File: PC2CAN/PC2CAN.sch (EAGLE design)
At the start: 97 parts, among them J11 M10X2, Q1 INFINEON_2N7002_DW, Q2 INFINEON_2N7002_DW, Q3 BS250F, Q4 BS250F, Q5 INFINEON_2N7002_DW, Q6 INFINEON_2N7002_DW, Q7 INFINEON_2N7002_DW, U1 MSP430F5521/5/7/9_PN80, U2 LTV-817, U3 SN74LV74, U4 SN74LV08

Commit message: Removed irrelevant circuits for PC2CAN and Power Controller
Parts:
- removed C11, C12: 0.1uF, rcl:C-USC0603
- removed JP10, JP11, JP13: M023.5MM, SparkFun-Connectors:M023.5MM
- removed JP14, JP7: (no value), SparkFun-Connectors:M04SCREW
- removed JP15: (no value), SparkFun-Connectors:M07
- removed JP6: (no value), SparkFun-Connectors:M05LOCK
- removed JP8: M02LOCK, SparkFun-Connectors:M02LOCK
- removed LED10, LED11, LED8, LED9: (no value), SparkFun-LED:LED0603
- removed Q1, Q6, Q7: INFINEON_2N7002_DW, npol-discrete:INFINEON_2N7002_DW
- removed R13, R27, R28, R33, R34: 0, rcl:R-US_R0603
- removed R23, R24: 10k, rcl:R-US_R0603
- removed R29, R30, R31, R32: 1k, rcl:R-US_R0603
- removed U3: SN74LV74, npol-digital:SN74LV74
- removed U4: SN74LV08, npol-digital:SN74LV08
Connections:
- removed net DRILL_RELAY_1: JP14.4, Q6G$1.DRAIN
- removed net DRILL_RELAY_2: JP14.3, Q6G$2.DRAIN
- removed net DRILL_RELAY_3: JP14.2, Q7G$1.DRAIN
- removed net DRILL_RELAY_4: JP14.1, Q7G$2.DRAIN
- removed net ESTOP_RELAY: JP13.2, Q1G$1.SOURCE, Q1G$2.SOURCE
- removed net N$14: LED9.A, R30.1
- removed net N$20: U31.Q, U41.A
- removed net N$22: U31./Q, U42.B
- removed net N$23: U32.Q, U43.A
- removed net N$25: U32./Q, U44.B
- removed net N$26: R27.1, U31./PRE
- removed net N$27: R28.2, U31./CLR
- removed net N$28: R33.1, U32./PRE
- removed net N$29: R34.2, U32./CLR
- removed net N$33: LED11.A, R32.1
- removed net RC_PWR: JP6.2, JP8.1
- removed net RC_S3: JP6.5, R13.2
- removed net RELAY1_CNTRL: Q6G$1.GATE, R29.2, U41.Y
- removed net RELAY1_LED_A: LED8.A, R29.1
- removed net RELAY2_CNTRL: Q6G$2.GATE, R30.2, U42.Y
- removed net RELAY3_CNTRL: Q7G$1.GATE, R31.2, U43.Y
- removed net RELAY3_LED_A: LED10.A, R31.1
- removed net RELAY4_CNTRL: Q7G$2.GATE, R32.2, U44.Y
- removed net VOC: JP15.7
- net +12V: no longer JP13.1
- net +3V3: no longer C11.1, C12.1, JP15.2, R23.2, R24.2, R27.2, R28.1, R33.2, R34.1, U31.VCC, U41.VCC
- net +5V: no longer JP7.4, JP8.2
- net DRILL_EN: no longer U31.CLK, U32.CLK, U41.B, U42.A, U43.B, U44.A
- net DRILL_ISENSE_/FAULT: no longer JP15.5
- net DRILL_ISENSE_FAULT_EN: no longer JP15.6
- net DRILL_ISENSE_VIOUT: no longer JP15.3
- net DRILL_ISENSE_VZCR: no longer JP15.4
- net DRILL_S1: no longer U31.D
- net DRILL_S2: no longer U32.D
- net ESTOP_LOCAL: no longer Q1G$1.GATE, Q1G$2.GATE, R13.1
- net GND: no longer C11.2, C12.2, JP10.1, JP11.1, JP15.1, JP6.1, LED10.C, LED11.C, LED8.C, LED9.C, Q1G$1.DRAIN, Q1G$2.DRAIN, Q6G$1.SOURCE, Q6G$2.SOURCE, Q7G$1.SOURCE, Q7G$2.SOURCE, U31.GND, U41.GND
- net LOWER_SWITCH: no longer JP11.2, R24.1
- net RC_S1: no longer JP6.3
- net RC_S2: no longer JP6.4
- net STEPPER_DIR: no longer JP7.2
- net STEPPER_EN: no longer JP7.3
- net STEPPER_STEP: no longer JP7.1
- net UPPER_SWITCH: no longer JP10.2, R23.1
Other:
- note added: "TODO: FTDI"
- note removed: "ACS709 Current Sensor"
- note removed: "ESTOP Relay Output shared with Drill and Stepper ESTOP relays"
- note removed: "Limit switches"
- note removed: "Roboclaw"
- note removed: "Stepper driver"
- note removed: "VOC Unused"

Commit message: PC2CAN ready for fab
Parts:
- removed JP12: M02LOCK, SparkFun-Connectors:M02LOCK
- removed Q5: INFINEON_2N7002_DW, npol-discrete:INFINEON_2N7002_DW
- added C11: 10nF, rcl:C-USC0603
- added C12: 0.1uF, rcl:C-USC0603
- added JP6: (no value), SparkFun-Connectors:M03LOCK
- added JP7: USB-B, SparkFun-Connectors:USBPTH
- added JP8: M02POLAR_LOCK, SparkFun-Connectors:M02POLAR_LOCK
- added LED10, LED8, LED9: (no value), SparkFun-LED:LED0603
- added Q1: INFINEON_2N7002_DW, npol-discrete:INFINEON_2N7002_DW
- added R13, R23: 10k, rcl:R-US_R0603
- added R24: 620, rcl:R-US_R0603
- added U3: LTV-817, npol-digital:LTV-817
- JP1: device SparkFun-Connectors:M03X22X3_SILK_SM -> SparkFun-Connectors:M05PTH
- JP2: value M02LOCK -> (none); device SparkFun-Connectors:M02LOCK -> SparkFun-Connectors:M03X22X3_SILK_SM
- JP3: value ONSHORE_OST302-S141 -> M02LOCK; device npol-connectors:ONSHORE_OST302-S141 -> SparkFun-Connectors:M02LOCK
- JP4: value FTDI_DEVICE -> ONSHORE_OST302-S141; device SparkFun-Connectors:FTDI_DEVICE -> npol-connectors:ONSHORE_OST302-S141
- JP5: value (none) -> FTDI_DEVICE; device SparkFun-Connectors:M03LOCK -> SparkFun-Connectors:FTDI_DEVICE
- JP9: value M02POLAR_LOCK -> M02LOCK; device SparkFun-Connectors:M02POLAR_LOCK -> SparkFun-Connectors:M02LOCK
- Q2: value INFINEON_2N7002_DW -> BS250F; device npol-discrete:INFINEON_2N7002_DW -> SparkFun-DiscreteSemi:MOSFET-PCHANNELSMD
- Q4: value BS250F -> INFINEON_2N7002_DW; device SparkFun-DiscreteSemi:MOSFET-PCHANNELSMD -> npol-discrete:INFINEON_2N7002_DW
- R15, R17: value 10k -> 470
- R18, R21: value 100k -> 10k
- R20, R22: value 10k -> 100k
- R25: value 620 -> 10k
- U2: value LTV-817 -> FT232RLSSOP; device npol-digital:LTV-817 -> SparkFun-DigitalIC:FT232RLSSOP
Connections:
- removed net DRILL_EN: U1.P7.6/TB0.4
- removed net DRILL_ISENSE_/FAULT: U1.P1.3/TA0.2
- removed net DRILL_ISENSE_FAULT_EN: U1.P6.0/CB0/A0
- removed net DRILL_ISENSE_VIOUT: U1.P6.2/CB2/A2
- removed net DRILL_ISENSE_VZCR: U1.P6.1/CB1/A1
- removed net DRILL_S1: U1.P7.5/TB0.3
- removed net DRILL_S2: U1.P7.4/TB0.2
- removed net LOWER_SWITCH: U1.P2.0/TA1.1
- removed net RC_RXD: R14.2, SJ3.3, SJ4.1, U1.P4.5/PM_UCA1RXD/PM_UCA1SOMI
- removed net RC_S1: SJ3.2
- removed net RC_S2: SJ4.2
- removed net RC_TXD: R15.2, SJ3.1, SJ4.3, U1.P4.4/PM_UCA1TXD/PM_UCA1SIMO
- removed net STEPPER_DIR: U1.P7.1/CB9/A13
- removed net STEPPER_EN: U1.P7.2/CB10/A14
- removed net STEPPER_STEP: U1.P1.2/TA0.1
- removed net UPPER_SWITCH: U1.P2.1/TA1.2
- new net N$14: JP7.D+, U2.USBDP
- new net N$15: JP7.D-, U2.USBDM
- new net N$16: LED8.C, R15.2
- new net N$17: LED9.C, R17.2
- new net N$18: R15.1, U2.TXLED
- new net N$19: R17.1, U2.RXLED
- new net N$20: C12.1, U2.3V3OUT
- new net N$21: Q4G$2.DRAIN, R26.2
- new net N$22: LED10.C, R26.1
- new net NU_P3.7: JP1.5, U1.P3.7/TB0OUTH/SVMOUT
- new net NU_P4.0: JP1.4, U1.P4.0/PM_UCB1STE/PM_UCA1CLK
- new net NU_P4.1: JP1.3, U1.P4.1/PM_UCB1SIMO/PM_UCB1SDA
- new net NU_P4.2: JP1.2, U1.P4.2/PM_UCB1SOMI/PM_UCB1SCL
- new net NU_P4.3: JP1.1, U1.P4.3/PM_UCB1CLK/PM_UCA1STE
- new net USB_RX: SJ3.2, U2.TXD
- new net USB_RXD: R13.2, SJ3.3, SJ4.1, U1.P4.5/PM_UCA1RXD/PM_UCA1SOMI
- new net USB_TX: SJ4.2, U2.RXD
- new net USB_TXD: R14.2, SJ3.1, SJ4.3, U1.P4.4/PM_UCA1TXD/PM_UCA1SIMO
- new net VBUS: C11.1, JP7.VBUS, LED8.A, LED9.A, U2.VCC, U2.VCCIO
- net +12V: now also Q3.S, R21.2; no longer Q4.S, R20.2
- net +3V3: now also JP3.1, JP6.2, LED10.A, R25.1; no longer JP2.1, JP5.2, R26.1
- net +5V: now also Q2.S, R18.2; no longer Q3.S, R17.2
- net 12VSENSE: now also R22.1, R23.2; no longer R21.1, R22.2
- net 5VSENSE: now also R19.1, R20.2; no longer R18.1, R19.2
- net ESTOP+: now also JP8.1, R24.2; no longer JP9.1, R25.2
- net ESTOP-: now also JP8.2, U3.2; no longer JP9.2, U2.2
- net ESTOP_LOCAL: now also JP9.1, Q4G$1.DRAIN, Q4G$2.GATE, R25.2; no longer JP12.1, Q5G$1.DRAIN, R26.2
- net ESTOP_LOCAL_INV: now also Q4G$1.GATE, U3.4; no longer Q5G$1.GATE, U2.4
- net GND: now also C11.2, C12.2, JP2.2, JP4.9, JP5.GND, JP7.GND, JP9.2, Q1G$1.SOURCE, Q1G$2.SOURCE, Q4G$1.SOURCE, Q4G$2.SOURCE, R13.1, R20.1, R23.1, U2.AGND, U2.GND18, U2.GND21, U2.GND7, U2.TEST, U3.3; no longer JP1.2, JP12.2, JP3.9, JP4.GND, Q2G$1.SOURCE, Q2G$2.SOURCE, Q5G$1.SOURCE, R15.1, R19.1, R22.1, U2.3
- net N$1: now also JP3.2, JP5.VCC; no longer JP2.2, JP4.VCC
- net N$10: now also Q1G$1.DRAIN, Q2.G, R18.1; no longer Q2G$1.DRAIN, Q3.G, R17.1
- net N$11: now also Q3.D, R22.2; no longer Q4.D, R21.2
- net N$12: now also Q1G$1.GATE, Q1G$2.GATE; no longer Q2G$1.GATE, Q2G$2.GATE
- net N$13: now also R24.1, U3.1; no longer R25.1, U2.1
- net N$9: now also Q2.D, R19.2; no longer Q3.D, R18.2
- net NU_P6.3: now also JP2.5; no longer JP1.5
- net NU_P6.4: now also JP2.6; no longer JP1.6
- net NU_P6.5: now also JP2.3; no longer JP1.3
- net NU_P6.6: now also JP2.4; no longer JP1.4
- net NU_P6.7: now also JP2.1; no longer JP1.1
- net RXI: now also JP5.RXI; no longer JP4.RXI
- net SBWTCK: now also JP4.7; no longer JP3.7
- net SBWTDIO: now also JP4.1; no longer JP3.1
- net TXO: now also JP5.TXO; no longer JP4.TXO
- net VCC_TARGET: now also JP4.4, JP6.1; no longer JP3.4, JP5.1
- net VCC_TOOL: now also JP4.2, JP6.3; no longer JP3.2, JP5.3
- net VTAP_EN: now also Q1G$2.DRAIN, Q3.G, R21.1; no longer Q2G$2.DRAIN, Q4.G, R20.1
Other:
- note removed: "TODO: FTDI"
- moved on the sheet: JP9, Q3, R14, R15, R17, R18, R19, R20, R21, R22, R25, R26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

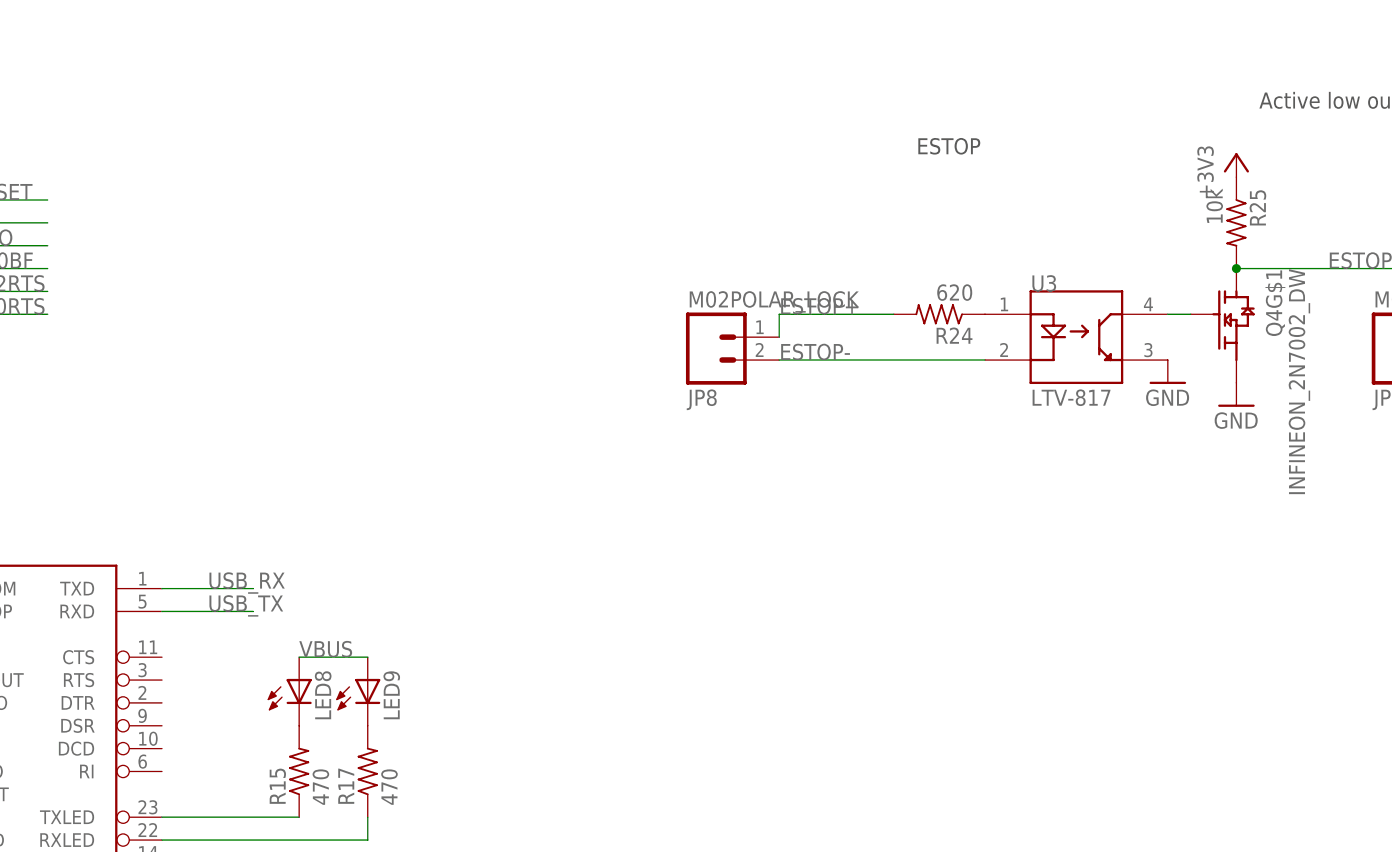
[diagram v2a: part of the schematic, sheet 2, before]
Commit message: Power Controller, Elim-Mobility Controller, and PC2CAN sent to FAB
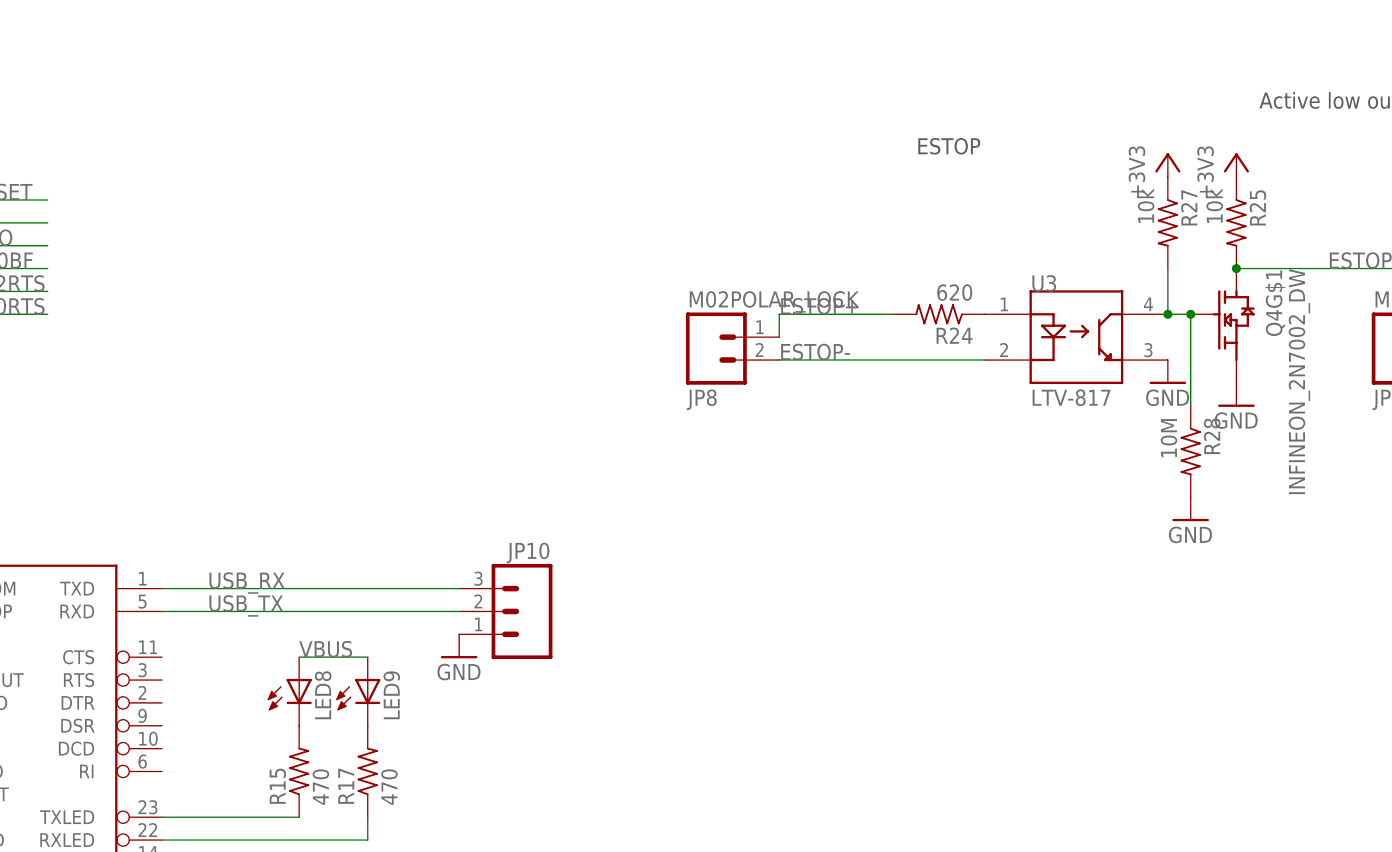
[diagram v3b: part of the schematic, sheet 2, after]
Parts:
- added JP10: (no value), SparkFun-Connectors:M03LOCK
- added R27: 10k, rcl:R-US_R0603
- added R28: 10M, rcl:R-US_R0603
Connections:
- net +3V3: now also R27.1
- net ESTOP_LOCAL_INV: now also R27.2, R28.1
- net GND: now also JP10.1, R28.2
- net USB_RX: now also JP10.3
- net USB_TX: now also JP10.2
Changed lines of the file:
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@@
 <grid distance="0.1" unitdist="inch" unit="inch" style="lines" multiple="1" display="no" altdistance="0.01" altunitdist="inch" altunit="inch"/>
 <layers>
-<layer number="1" name="Top" color="4" fill="1" visible="yes" active="no"/>
-<layer number="2" name="Route2" color="1" fill="3" visible="yes" active="no"/>
-<layer number="3" name="Route3" color="4" fill="3" visible="yes" active="no"/>
-<layer number="14" name="Route14" color="1" fill="6" visible="yes" active="no"/>
-<layer number="15" name="Route15" color="4" fill="6" visible="yes" active="no"/>
-<layer number="16" name="Bottom" color="1" fill="1" visible="yes" active="no"/>
-<layer number="17" name="Pads" color="2" fill="1" visible="yes" active="no"/>
-<layer number="18" name="Vias" color="2" fill="1" visible="yes" active="no"/>
-<layer number="19" name="Unrouted" color="6" fill="1" visible="yes" active="no"/>
-<layer number="20" name="Dimension" color="15" fill="1" visible="yes" active="no"/>
-<layer number="21" name="tPlace" color="7" fill="1" visible="yes" active="no"/>
-<layer number="22" name="bPlace" color="7" fill="1" visible="yes" active="no"/>
-<layer number="23" name="tOrigins" color="15" fill="1" visible="yes" active="no"/>
-<layer number="24" name="bOrigins" color="15" fill="1" visible="yes" active="no"/>
-<layer number="25" name="tNames" color="7" fill="1" visible="yes" active="no"/>
-<layer number="26" name="bNames" color="7" fill="1" visible="yes" active="no"/>
-<layer number="27" name="tValues" color="7" fill="1" visible="yes" active="no"/>
-<layer number="28" name="bValues" color="7" fill="1" visible="yes" active="no"/>
+<layer number="1" name="Top" color="4" fill="1" visible="no" active="no"/>
+<layer number="2" name="Route2" color="1" fill="3" visible="no" active="no"/>
+<layer number="3" name="Route3" color="4" fill="3" visible="no" active="no"/>
+<layer number="14" name="Route14" color="1" fill="6" visible="no" active="no"/>
+<layer number="15" name="Route15" color="4" fill="6" visible="no" active="no"/>
+<layer number="16" name="Bottom" color="1" fill="1" visible="no" active="no"/>
+<layer number="17" name="Pads" color="2" fill="1" visible="no" active="no"/>
+<layer number="18" name="Vias" color="2" fill="1" visible="no" active="no"/>
+<layer number="19" name="Unrouted" color="6" fill="1" visible="no" active="no"/>
+<layer number="20" name="Dimension" color="15" fill="1" visible="no" active="no"/>
+<layer number="21" name="tPlace" color="7" fill="1" visible="no" active="no"/>
+<layer number="22" name="bPlace" color="7" fill="1" visible="no" active="no"/>
+<layer number="23" name="tOrigins" color="15" fill="1" visible="no" active="no"/>
+<layer number="24" name="bOrigins" color="15" fill="1" visible="no" active="no"/>
+<layer number="25" name="tNames" color="7" fill="1" visible="no" active="no"/>
+<layer number="26" name="bNames" color="7" fill="1" visible="no" active="no"/>
+<layer number="27" name="tValues" color="7" fill="1" visible="no" active="no"/>
+<layer number="28" name="bValues" color="7" fill="1" visible="no" active="no"/>
 <layer number="29" name="tStop" color="7" fill="3" visible="no" active="no"/>
 <layer number="30" name="bStop" color="7" fill="6" visible="no" active="no"/>
@@
 <layer number="35" name="tGlue" color="7" fill="4" visible="no" active="no"/>
 <layer number="36" name="bGlue" color="7" fill="5" visible="no" active="no"/>
-<layer number="37" name="tTest" color="7" fill="1" visible="yes" active="no"/>
-<layer number="38" name="bTest" color="7" fill="1" visible="yes" active="no"/>
+<layer number="37" name="tTest" color="7" fill="1" visible="no" active="no"/>
+<layer number="38" name="bTest" color="7" fill="1" visible="no" active="no"/>
 <layer number="39" name="tKeepout" color="4" fill="11" visible="no" active="no"/>
 <layer number="40" name="bKeepout" color="1" fill="11" visible="no" active="no"/>
@@
 <layer number="44" name="Drills" color="7" fill="1" visible="no" active="no"/>
 <layer number="45" name="Holes" color="7" fill="1" visible="no" active="no"/>
-<layer number="46" name="Milling" color="3" fill="1" visible="yes" active="no"/>
-<layer number="47" name="Measures" color="7" fill="1" visible="yes" active="no"/>
-<layer number="48" name="Document" color="7" fill="1" visible="yes" active="no"/>
-<layer number="49" name="Reference" color="7" fill="1" visible="yes" active="no"/>
-<layer number="50" name="dxf" color="7" fill="1" visible="yes" active="no"/>
-<layer number="51" name="tDocu" color="7" fill="1" visible="yes" active="no"/>
-<layer number="52" name="bDocu" color="7" fill="1" visible="yes" active="no"/>
-<layer number="53" name="tGND_GNDA" color="7" fill="9" visible="yes" active="no"/>
-<layer number="54" name="bGND_GNDA" color="1" fill="9" visible="yes" active="no"/>
-<layer number="56" name="wert" color="7" fill="1" visible="yes" active="no"/>
-<layer number="57" name="tCAD" color="7" fill="1" visible="yes" active="no"/>
-<layer number="59" name="tCarbon" color="7" fill="1" visible="yes" active="no"/>
-<layer number="60" name="bCarbon" color="7" fill="1" visible="yes" active="no"/>
+<layer number="46" name="Milling" color="3" fill="1" visible="no" active="no"/>
+<layer number="47" name="Measures" color="7" fill="1" visible="no" active="no"/>
+<layer number="48" name="Document" color="7" fill="1" visible="no" active="no"/>
+<layer number="49" name="Reference" color="7" fill="1" visible="no" active="no"/>
+<layer number="50" name="dxf" color="7" fill="1" visible="no" active="no"/>
+<layer number="51" name="tDocu" color="7" fill="1" visible="no" active="no"/>
+<layer number="52" name="bDocu" color="7" fill="1" visible="no" active="no"/>
+<layer number="53" name="tGND_GNDA" color="7" fill="9" visible="no" active="no"/>
+<layer number="54" name="bGND_GNDA" color="1" fill="9" visible="no" active="no"/>
+<layer number="56" name="wert" color="7" fill="1" visible="no" active="no"/>
+<layer number="57" name="tCAD" color="7" fill="1" visible="no" active="no"/>
+<layer number="59" name="tCarbon" color="7" fill="1" visible="no" active="no"/>
+<layer number="60" name="bCarbon" color="7" fill="1" visible="no" active="no"/>
 <layer number="91" name="Nets" color="2" fill="1" visible="yes" active="yes"/>
 <layer number="92" name="Busses" color="1" fill="1" visible="yes" active="yes"/>
@@
 <part name="+3V39" library="supply1" deviceset="+3V3" device=""/>
 <part name="R26" library="rcl" deviceset="R-US_" device="R0603" value="10k"/>
+<part name="R27" library="rcl" deviceset="R-US_" device="R0603" value="10k"/>
+<part name="R28" library="rcl" deviceset="R-US_" device="R0603" value="10M"/>
+<part name="GND40" library="supply1" deviceset="GND" device=""/>
+<part name="+3V1" library="supply1" deviceset="+3V3" device=""/>
+<part name="JP10" library="SparkFun-Connectors" deviceset="M03" device="LOCK"/>
+<part name="GND41" library="supply1" deviceset="GND" device=""/>
 </parts>
 <sheets>
@@
 <instance part="+3V39" gate="G$1" x="248.92" y="208.28"/>
 <instance part="R26" gate="G$1" x="248.92" y="193.04" rot="R270"/>
+<instance part="R27" gate="G$1" x="200.66" y="187.96" rot="R270"/>
+<instance part="R28" gate="G$1" x="203.2" y="162.56" rot="R270"/>
+<instance part="GND40" gate="1" x="203.2" y="154.94"/>
+<instance part="+3V1" gate="G$1" x="200.66" y="195.58"/>
+<instance part="JP10" gate="G$1" x="129.54" y="144.78" rot="MR0"/>
+<instance part="GND41" gate="1" x="121.92" y="139.7"/>
 </instances>
 <busses>
@@
 <pinref part="GND39" gate="1" pin="GND"/>
 </segment>
+<segment>
+<pinref part="R28" gate="G$1" pin="2"/>
+<pinref part="GND40" gate="1" pin="GND"/>
+</segment>
+<segment>
+<pinref part="JP10" gate="G$1" pin="1"/>
+<pinref part="GND41" gate="1" pin="GND"/>
+</segment>
 </net>
 <net name="CAN_STBY" class="0">
@@
 <pinref part="+3V39" gate="G$1" pin="+3V3"/>
 <pinref part="LED10" gate="G$1" pin="A"/>
+</segment>
+<segment>
+<pinref part="R27" gate="G$1" pin="1"/>
+<pinref part="+3V1" gate="G$1" pin="+3V3"/>
 </segment>
 </net>
@@
 <wire x1="200.66" y1="177.8" x2="203.2" y2="177.8" width="0.1524" layer="91"/>
 <pinref part="Q4" gate="G$1" pin="GATE"/>
+<pinref part="R27" gate="G$1" pin="2"/>
+<wire x1="200.66" y1="182.88" x2="200.66" y2="177.8" width="0.1524" layer="91"/>
+<junction x="200.66" y="177.8"/>
+<pinref part="R28" gate="G$1" pin="1"/>
+<wire x1="203.2" y1="177.8" x2="203.2" y2="167.64" width="0.1524" layer="91"/>
+<junction x="203.2" y="177.8"/>
 </segment>
 </net>
@@
 <segment>
 <pinref part="U2" gate="G$1" pin="TXD"/>
-<wire x1="88.9" y1="147.32" x2="99.06" y2="147.32" width="0.1524" layer="91"/>
 <label x="93.98" y="147.32" size="1.778" layer="95"/>
+<pinref part="JP10" gate="G$1" pin="3"/>
+<wire x1="88.9" y1="147.32" x2="121.92" y2="147.32" width="0.1524" layer="91"/>
 </segment>
 <segment>
@@
 <segment>
 <pinref part="U2" gate="G$1" pin="RXD"/>
-<wire x1="88.9" y1="144.78" x2="99.06" y2="144.78" width="0.1524" layer="91"/>
 <label x="93.98" y="144.78" size="1.778" layer="95"/>
-</segment>
-<segment>
+<pinref part="JP10" gate="G$1" pin="2"/>
+<wire x1="88.9" y1="144.78" x2="121.92" y2="144.78" width="0.1524" layer="91"/>
+</segment>
+<segment>
